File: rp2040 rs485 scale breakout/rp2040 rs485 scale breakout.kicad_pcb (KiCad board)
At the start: 2 copper layers, 123.2 x 50.2 mm, 97 parts, among them J1 main i2c, J10 i2c 3, J11 i2c 4, J12 i2c 2, J13 i2c 0, J14 i2c 1, J15 channel 1, J16 channel 2, J17 cap, J18 i2c pullips, J19 channel 1, J2 ESDU5V0H4, J20 channel 2, J21 cap, J22 i2c pullips, J3 rs485, J4 Conn_01x01, J5 i2c pullups, J6 qwiic from pro micro, J7 i2c 5, J8 i2c 6, J9 i2c 7, U1 MAX487E, U2 ProMicro_2040, U3 PCA9548ADW, U4 NAU7802SGI, U5 NAU7802SGI

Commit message: motor driver and scale pcb gerbers
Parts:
- added C24: 10uF, Capacitor_SMD:C_1206_3216Metric, F.Cu at (217.2, 119.9)
- added C25: 10uF, Capacitor_SMD:C_1206_3216Metric, F.Cu at (210.8, 107.4)
- added D1: 24v, LED_SMD:LED_0603_1608Metric, F.Cu at (238.5, 130.8)
- added D2: 5v, LED_SMD:LED_0603_1608Metric, F.Cu at (238.5, 127.5)
- added D3: 3.3v, LED_SMD:LED_0603_1608Metric, F.Cu at (238.5, 124.0)
- added J23: power in, TerminalBlock_Phoenix:TerminalBlock_Phoenix_MKDS-1,5-2_1x02_P5.00mm_Horizontal, F.Cu at (225.3, 135.6)
- added R41: 2.2K, Resistor_SMD:R_0603_1608Metric, F.Cu at (234.9, 130.8)
- added R42: 2.2K, Resistor_SMD:R_0603_1608Metric, F.Cu at (234.9, 127.5)
- added R43: 2.2K, Resistor_SMD:R_0603_1608Metric, F.Cu at (233.4, 121.2)
- added U6: mp1584 dcdc, Evan's misc parts:MP1584_buck_module, F.Cu at (227.1, 114.8)
- added U7: LD1117S33, Package_TO_SOT_SMD:SOT-223-3_TabPin2, F.Cu at (212.3, 113.3)
- U3: footprint Evan's misc parts:SOIC127P1030X265-24N -> Package_SO:TSSOP-24_4.4x7.8mm_P0.65mm
- moved C3 6.14 mm to (176.0, 111.0)
- moved U3 2.55 mm to (171.4, 116.3)
- moved R10 1.70 mm to (164.1, 110.7), turned to -90 degrees
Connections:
- J1 pad MP: (no net) -> GND
- J10 pad MP: (no net) -> GND
- J11 pad MP: (no net) -> GND
- J12 pad MP: (no net) -> GND
- J13 pad MP: (no net) -> GND
- J14 pad MP: (no net) -> GND
- J6 pad MP: (no net) -> GND
- J7 pad MP: (no net) -> GND
- J8 pad MP: (no net) -> GND
- J9 pad MP: (no net) -> GND
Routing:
- net +5V: track 0.00 -> 48.2 mm, vias 0 -> 2
- net +3V3: track 419.3 -> 452.9 mm, vias 26 -> 28
- net +24V: track 0.00 -> 18.3 mm
- net A0: track 22.5 -> 30.2 mm
- net A1: track 22.9 -> 29.6 mm
- net Net-(J4-Pad1): track 6.12 -> 12.0 mm
- net SCL1: track 53.0 -> 48.2 mm, vias 1 -> 2
- net Net-(D3-Pad2): track 0.00 -> 4.62 mm
- net Main_SCL: track 46.2 -> 50.4 mm
- net Main_SDA: track 48.7 -> 52.6 mm
- net SCL7: track 61.3 -> 65.2 mm
- net SDA7: track 63.4 -> 67.2 mm
- net A2: track 33.6 -> 37.1 mm
- net SDA0: track 21.4 -> 24.8 mm
- net SCL6: track 53.1 -> 56.5 mm
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
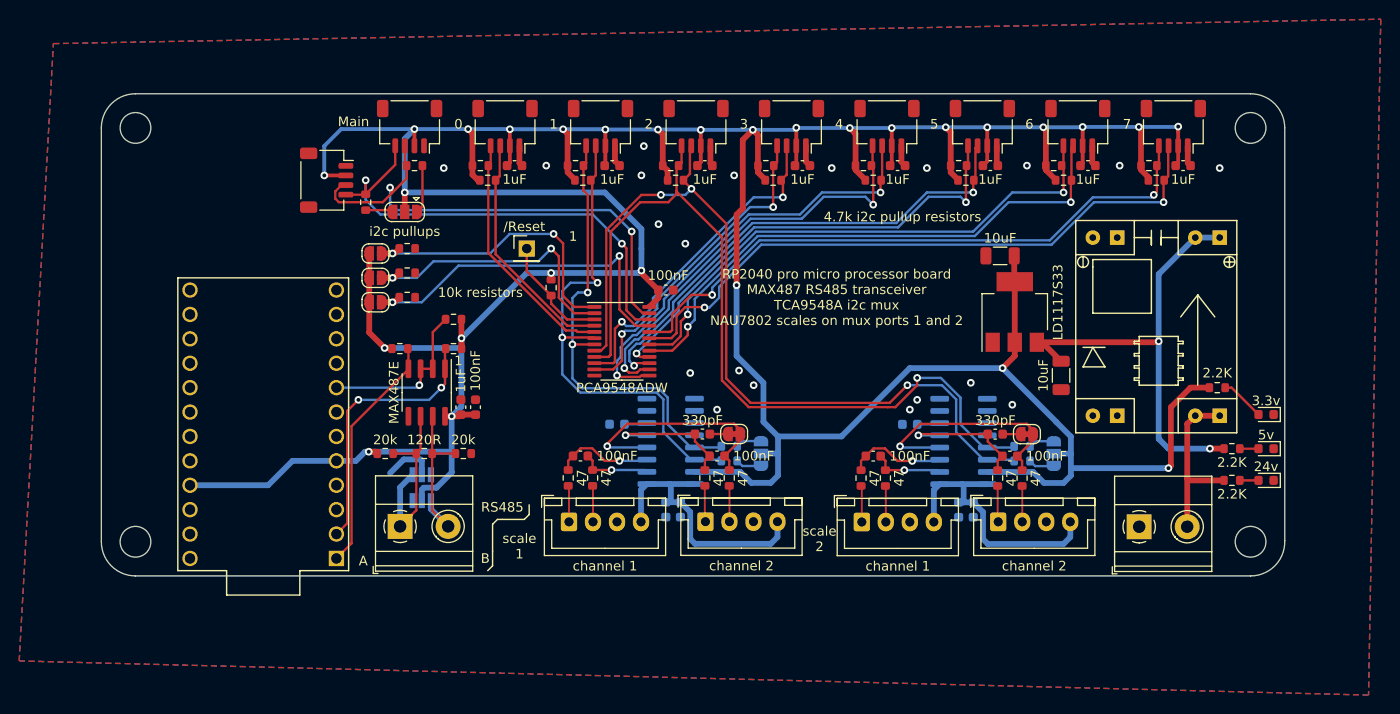
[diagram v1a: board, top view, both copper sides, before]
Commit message: tweaked buck converter hole sizes and silk
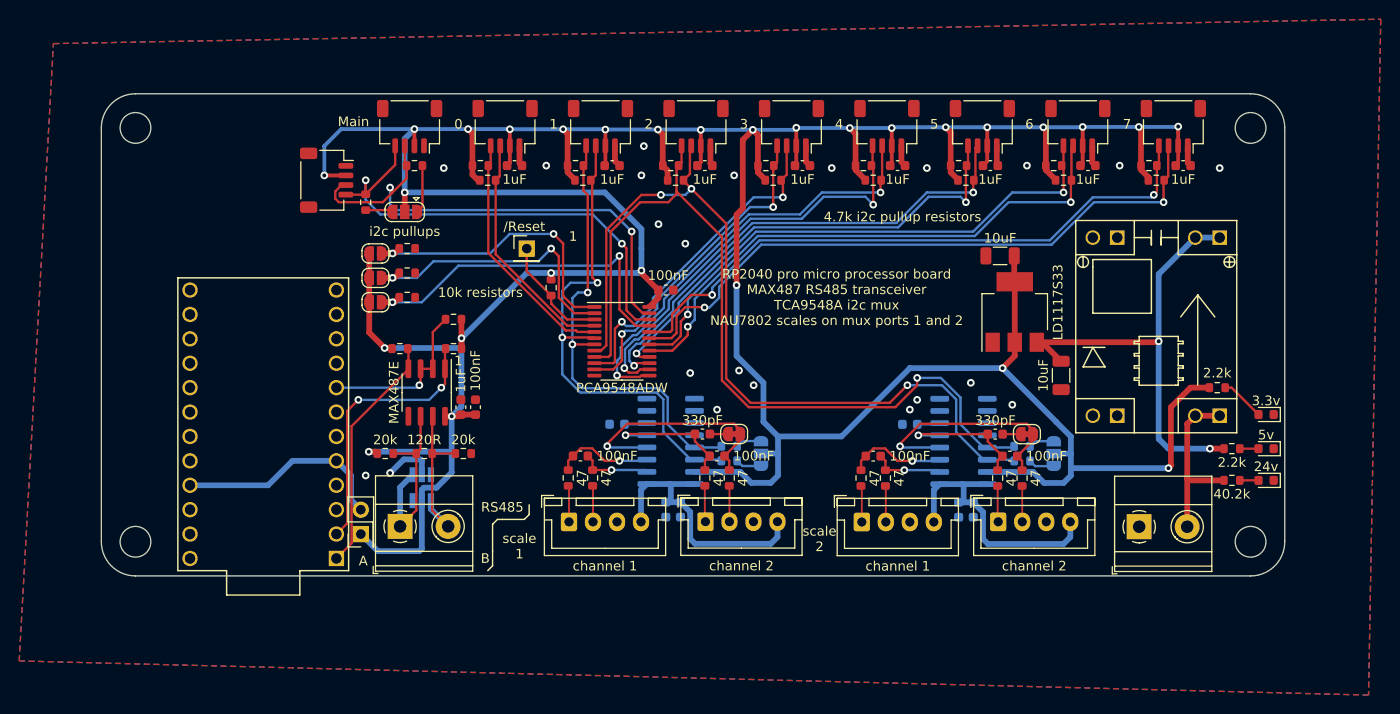
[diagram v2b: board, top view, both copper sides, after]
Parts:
- added J24: Conn_01x02, Connector_PinHeader_2.54mm:PinHeader_2x01_P2.54mm_Vertical, F.Cu at (144.3, 136.4)
- R41: value 2.2K -> 40.2k
- R42, R43: value 2.2K -> 2.2k
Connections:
- J1 pad MP: GND -> (no net)
- J10 pad MP: GND -> (no net)
- J11 pad MP: GND -> (no net)
- J12 pad MP: GND -> (no net)
- J13 pad MP: GND -> (no net)
- J14 pad MP: GND -> (no net)
- J6 pad MP: GND -> (no net)
- J7 pad MP: GND -> (no net)
- J8 pad MP: GND -> (no net)
- J9 pad MP: GND -> (no net)
- U2 pad 21: +3V3 -> Net-(U2-Pad21)
- U2 pad 5: +3V3 -> Net-(U2-Pad21)
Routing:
- net Net-(U2-Pad21): track 0.00 -> 22.4 mm
- net +3V3: track 452.9 -> 445.0 mm
- net GND: vias 20 -> 22
